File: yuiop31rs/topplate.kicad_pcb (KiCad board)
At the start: 2 copper layers, 118 x 118 mm, 36 parts, among them SW1 SW_PUSH, SW10 SW_PUSH, SW11 SW_PUSH, SW12 SW_PUSH, SW13 SW_PUSH, SW14 SW_PUSH, SW15 SW_PUSH, SW16 SW_PUSH, SW17 SW_PUSH, SW18 SW_PUSH, SW19 SW_PUSH, SW2 SW_PUSH, SW20 SW_PUSH, SW21 SW_PUSH, SW22 SW_PUSH, SW23 SW_PUSH, SW24 SW_PUSH, SW25 SW_PUSH, SW26 SW_PUSH, SW27 SW_PUSH, SW28 SW_PUSH, SW29 SW_PUSH, SW3 SW_PUSH, SW30 SW_PUSH, SW31 SW_PUSH, SW4 SW_PUSH, SW5 SW_PUSH, SW6 SW_PUSH, SW7 SW_PUSH, SW8 SW_PUSH, SW9 SW_PUSH

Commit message: yuiop31rs: fix circuit, generate gerbers
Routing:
- added copper zone on F.Cu, net (none)
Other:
- board text added: "JLCJLCJLCJLC"
- board text added: "YUIOP31RS"
- board text added: "designed by KoRoN/KaoriYa"
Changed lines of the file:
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@@
   (general
     (thickness 1.6)
-    (drawings 16)
+    (drawings 19)
     (tracks 0)
     (zones 0)
@@
       (outputformat 1)
       (mirror false)
-      (drillshape 1)
+      (drillshape 0)
       (scaleselection 1)
-      (outputdirectory ""))
+      (outputdirectory "gerbers/topplate-jlcpcb-r1/"))
   )
   (net 0 "")
@@
     (fp_arc (start -6.7 -6.7) (end -6.7 -7) (angle -90) (layer Edge.Cuts) (width 0.12))
     (fp_arc (start 6.7 -6.7) (end 7 -6.7) (angle -90) (layer Edge.Cuts) (width 0.12))
+  )
+  (gr_text JLCJLCJLCJLC (at 98 157) (layer B.SilkS)
+    (effects (font (size 0.8 0.8) (thickness 0.15)) (justify mirror))
+  )
+  (gr_text "designed by KoRoN/KaoriYa" (at 117 77) (layer F.Mask)
+    (effects (font (size 1 1) (thickness 0.15)))
+  )
+  (gr_text YUIOP31RS (at 112 72) (layer F.Mask)
+    (effects (font (size 6 4) (thickness 0.6)))
   )
   (gr_circle (center 108.55 48.95) (end 111.55 48.95) (layer Edge.Cuts) (width 0.05))
@@
   (gr_line (start 209 43) (end 209 157) (layer Edge.Cuts) (width 0.05))
   (gr_line (start 93 41) (end 207 41) (layer Edge.Cuts) (width 0.05))
+  (zone (net 0) (net_name "") (layer F.Cu) (hatch edge 0.508)
+    (connect_pads (clearance 0.508))
+    (min_thickness 0.254)
+    (fill yes (arc_segments 32) (thermal_gap 0.508) (thermal_bridge_width 0.508))
+    (polygon
+      (pts
+        (xy 209 159) (xy 91 159) (xy 91 41) (xy 209 41)
+      )
+    )
+  )
 )

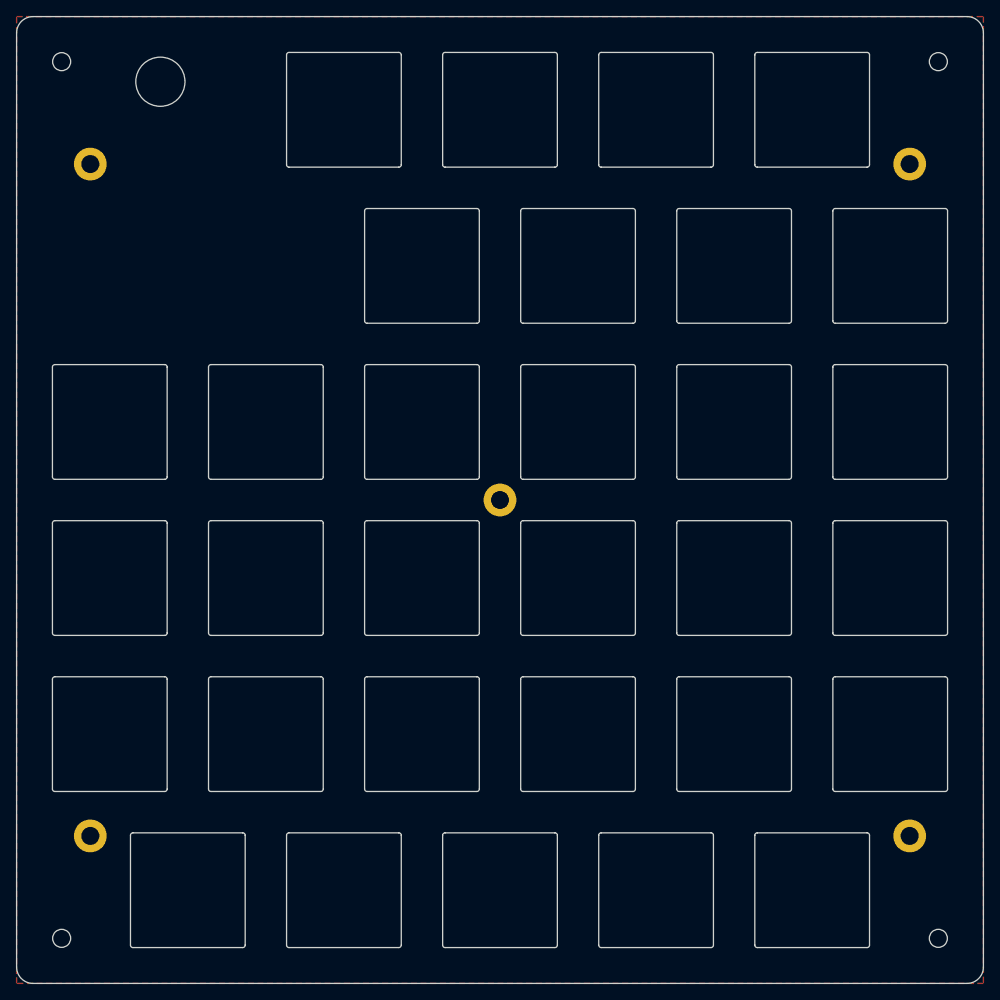
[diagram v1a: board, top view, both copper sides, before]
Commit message: convert topplate to KiCad 8.0
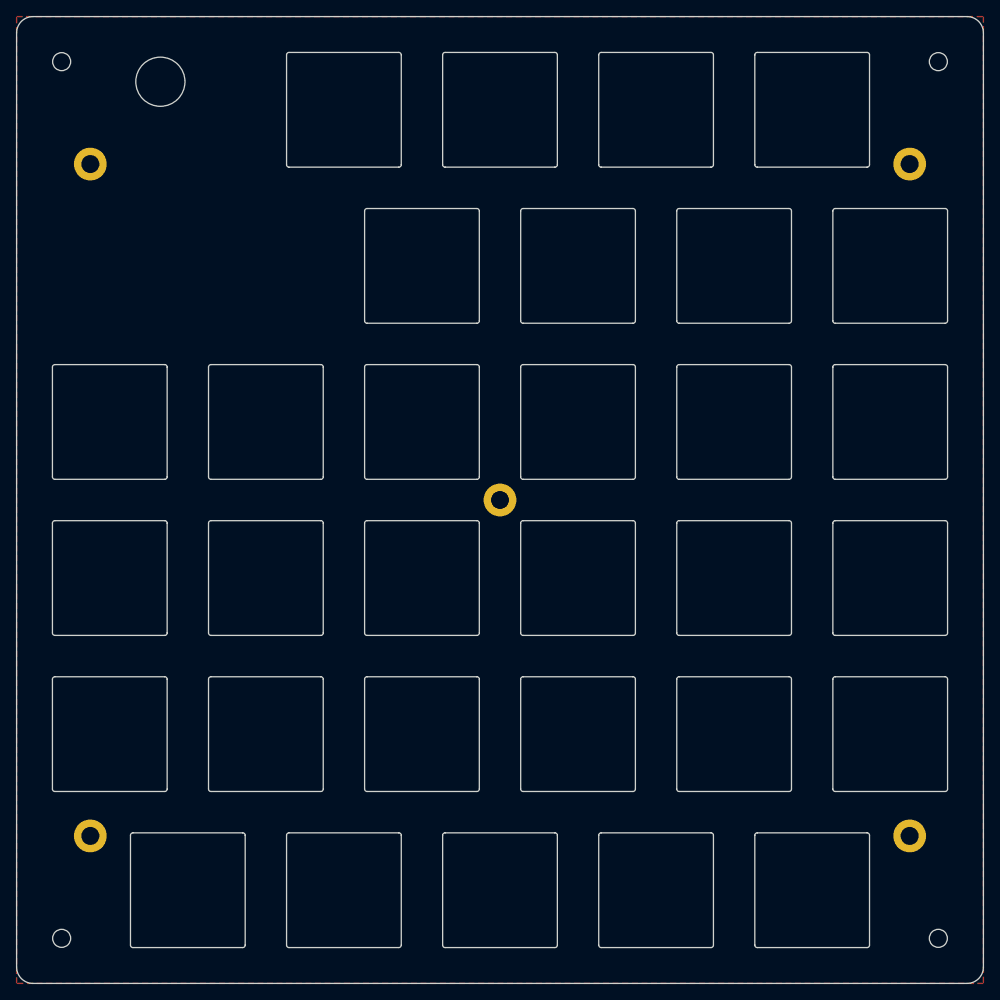
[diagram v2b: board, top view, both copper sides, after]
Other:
- net class Default removed
